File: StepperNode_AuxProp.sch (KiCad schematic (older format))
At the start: 4 parts

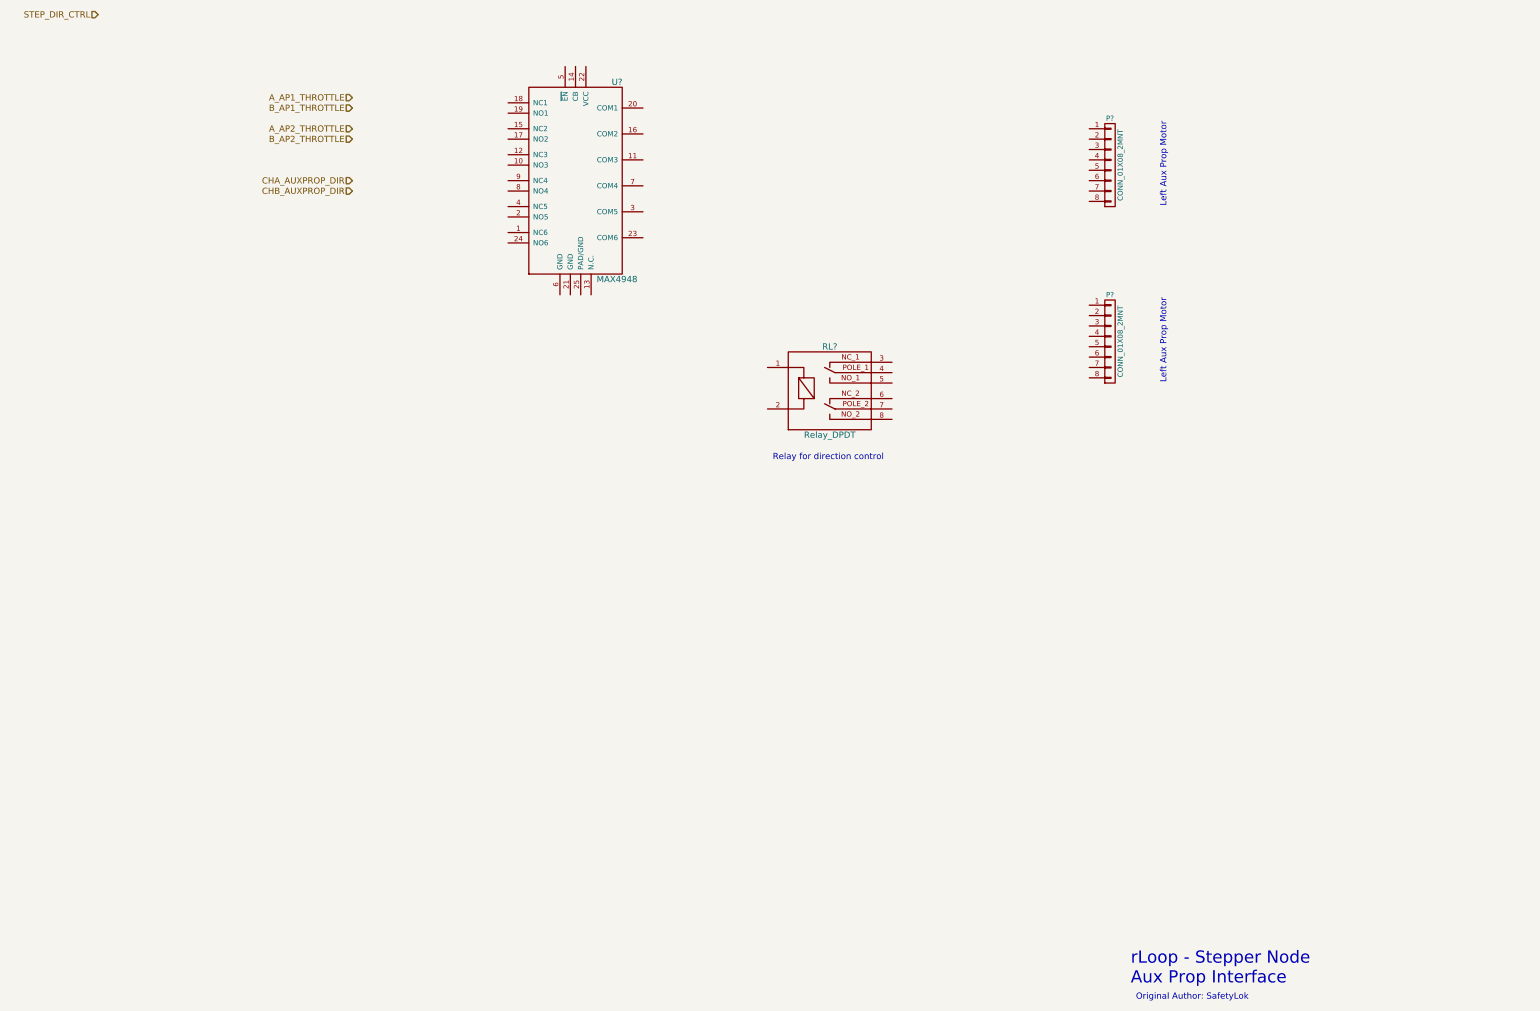
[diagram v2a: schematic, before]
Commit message: Update Stepper Temp Sensor Interface
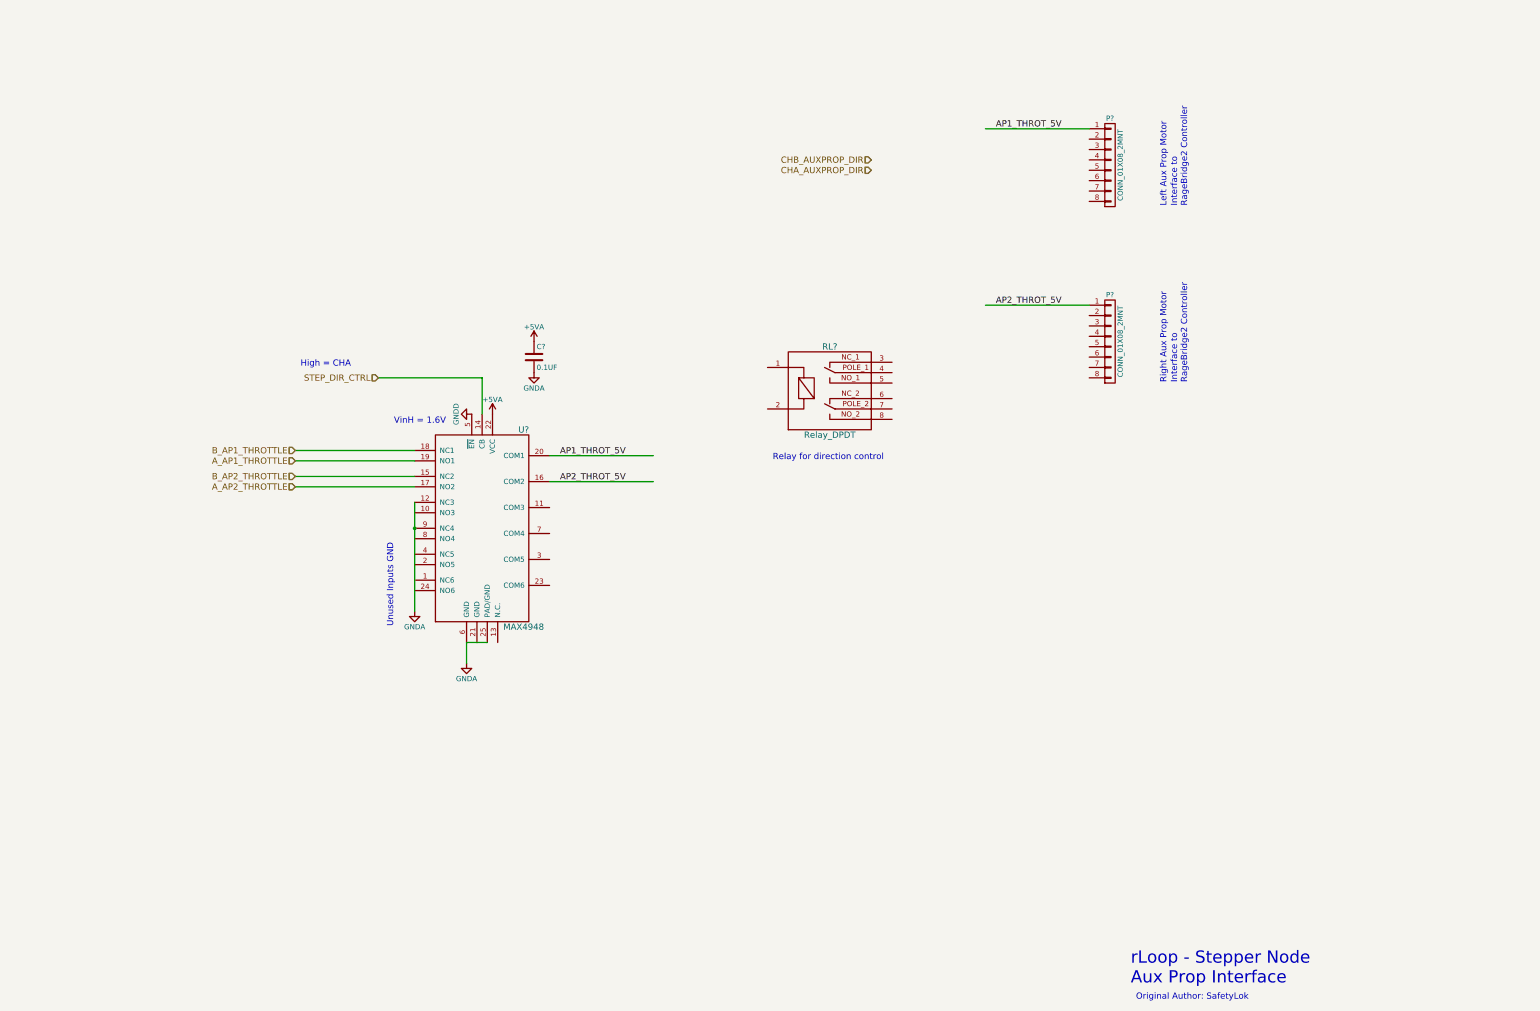
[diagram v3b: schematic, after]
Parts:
- added C?: 0.1UF, symbol C
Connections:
- net labels added: +5VA, AP1_THROT_5V, AP2_THROT_5V, GNDA, GNDD
- wire segments 0 -> 13
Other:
- note added: "High = CHA"
- note added: "Interface to \nRageBridge2 Controller"
- note added: "Right Aux Prop Motor"
- note added: "Unused Inputs GND"
- note added: "VinH = 1.6V"
- moved on the sheet: U?
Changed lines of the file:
@@
 $Descr A3 16535 11693
 encoding utf-8
-Sheet 16 17
+Sheet 15 17
 Title "Aux Propulsion Interface"
 Date ""
@@
 L MAX4948 U?
 U 1 1 575AE7BC
-P 6100 3500
-F 0 "U?" H 6950 5350 60  0000 C CNN
-F 1 "MAX4948" H 6950 3450 60  0000 C CNN
-F 2 "" H 6100 4250 60  0000 C CNN
-F 3 "" H 6100 4250 60  0000 C CNN
-	1    6100 3500
-	1    0    0    -1
-$EndComp
-Text HLabel 1950 1000 0    60   Input ~ 0
+P 5200 6850
+F 0 "U?" H 6050 8700 60  0000 C CNN
+F 1 "MAX4948" H 6050 6800 60  0000 C CNN
+F 2 "" H 5200 7600 60  0000 C CNN
+F 3 "" H 5200 7600 60  0000 C CNN
+	1    5200 6850
+	1    0    0    -1
+$EndComp
+Text HLabel 4650 4500 0    60   Input ~ 0
 STEP_DIR_CTRL
-Text HLabel 4400 1800 0    60   Input ~ 0
+Text HLabel 3850 5300 0    60   Input ~ 0
 A_AP1_THROTTLE
-Text HLabel 4400 1900 0    60   Input ~ 0
+Text HLabel 3850 5200 0    60   Input ~ 0
 B_AP1_THROTTLE
-Text HLabel 4400 2100 0    60   Input ~ 0
+Text HLabel 3850 5550 0    60   Input ~ 0
 A_AP2_THROTTLE
-Text HLabel 4400 2200 0    60   Input ~ 0
+Text HLabel 3850 5450 0    60   Input ~ 0
 B_AP2_THROTTLE
 $Comp
@@
 	1    0    0    -1
 $EndComp
-Text Notes 12250 4550 1    60   ~ 0
-Left Aux Prop Motor
 $Comp
 L Relay_DPDT RL?
@@
 Text Notes 8450 5300 0    60   ~ 0
 Relay for direction control
-Text HLabel 4400 2600 0    60   Input ~ 0
+Text HLabel 9400 2500 0    60   Input ~ 0
 CHA_AUXPROP_DIR
-Text HLabel 4400 2700 0    60   Input ~ 0
+Text HLabel 9400 2400 0    60   Input ~ 0
 CHB_AUXPROP_DIR
+$Comp
+L +5VA #PWR?
+U 1 1 5756511D
+P 5750 4850
+F 0 "#PWR?" H 5750 4700 50  0001 C CNN
+F 1 "+5VA" H 5750 4990 50  0000 C CNN
+F 2 "" H 5750 4850 50  0000 C CNN
+F 3 "" H 5750 4850 50  0000 C CNN
+	1    5750 4850
+	1    0    0    -1
+$EndComp
+$Comp
+L C C?
+U 1 1 57565139
+P 6150 4300
+F 0 "C?" H 6175 4400 50  0000 L CNN
+F 1 "0.1UF" H 6175 4200 50  0000 L CNN
+F 2 "" H 6188 4150 50  0000 C CNN
+F 3 "" H 6150 4300 50  0000 C CNN
+	1    6150 4300
+	1    0    0    -1
+$EndComp
+$Comp
+L +5VA #PWR?
+U 1 1 575651A0
+P 6150 4150
+F 0 "#PWR?" H 6150 4000 50  0001 C CNN
+F 1 "+5VA" H 6150 4290 50  0000 C CNN
+F 2 "" H 6150 4150 50  0000 C CNN
+F 3 "" H 6150 4150 50  0000 C CNN
+	1    6150 4150
+	1    0    0    -1
+$EndComp
+$Comp
+L GNDA #PWR?
+U 1 1 575651AF
+P 5000 6750
+F 0 "#PWR?" H 5000 6500 50  0001 C CNN
+F 1 "GNDA" H 5000 6600 50  0000 C CNN
+F 2 "" H 5000 6750 50  0000 C CNN
+F 3 "" H 5000 6750 50  0000 C CNN
+	1    5000 6750
+	1    0    0    -1
+$EndComp
+Text Notes 4800 4950 0    60   ~ 0
+VinH = 1.6V
+$Comp
+L GNDD #PWR?
+U 1 1 57565359
+P 5550 4850
+F 0 "#PWR?" H 5550 4600 50  0001 C CNN
+F 1 "GNDD" H 5550 4700 50  0000 C CNN
+F 2 "" H 5550 4850 50  0000 C CNN
+F 3 "" H 5550 4850 50  0000 C CNN
+	1    5550 4850
+	0    1    1    0
+$EndComp
+Wire Wire Line
+	5650 4850 5650 4500
+Wire Wire Line
+	5650 4500 4650 4500
+Text Notes 3900 4400 0    60   ~ 0
+High = CHA
+Wire Wire Line
+	5000 5200 3850 5200
+Wire Wire Line
+	5000 5300 3850 5300
+Wire Wire Line
+	5000 5450 3850 5450
+Wire Wire Line
+	5000 5550 3850 5550
+Wire Wire Line
+	5700 7050 5500 7050
+Wire Wire Line
+	5500 7050 5500 7250
+Wire Wire Line
+	5000 5700 5000 6750
+Text Notes 4800 6900 1    60   ~ 0
+Unused Inputs GND
+$Comp
+L GNDA #PWR?
+U 1 1 5756652B
+P 6150 4450
+F 0 "#PWR?" H 6150 4200 50  0001 C CNN
+F 1 "GNDA" H 6150 4300 50  0000 C CNN
+F 2 "" H 6150 4450 50  0000 C CNN
+F 3 "" H 6150 4450 50  0000 C CNN
+	1    6150 4450
+	1    0    0    -1
+$EndComp
+$Comp
+L GNDA #PWR?
+U 1 1 5756673C
+P 5500 7250
+F 0 "#PWR?" H 5500 7000 50  0001 C CNN
+F 1 "GNDA" H 5500 7100 50  0000 C CNN
+F 2 "" H 5500 7250 50  0000 C CNN
+F 3 "" H 5500 7250 50  0000 C CNN
+	1    5500 7250
+	1    0    0    -1
+$EndComp
+Text Notes 12450 2850 1    60   ~ 0
+Interface to \nRageBridge2 Controller
+Text Notes 12250 4550 1    60   ~ 0
+Right Aux Prop Motor
+Text Notes 12450 4550 1    60   ~ 0
+Interface to \nRageBridge2 Controller
+Connection ~ 5000 5950
+Wire Wire Line
+	6300 5250 7300 5250
+Text Label 6400 5250 0    60   ~ 0
+AP1_THROT_5V
+Wire Wire Line
+	6300 5500 7300 5500
+Text Label 6400 5500 0    60   ~ 0
+AP2_THROT_5V
+Wire Wire Line
+	10500 2100 11500 2100
+Text Label 10600 2100 0    60   ~ 0
+AP1_THROT_5V
+Wire Wire Line
+	10500 3800 11500 3800
+Text Label 10600 3800 0    60   ~ 0
+AP2_THROT_5V
 $EndSCHEMATC

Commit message: Updated node core connector pages and added interlocks.
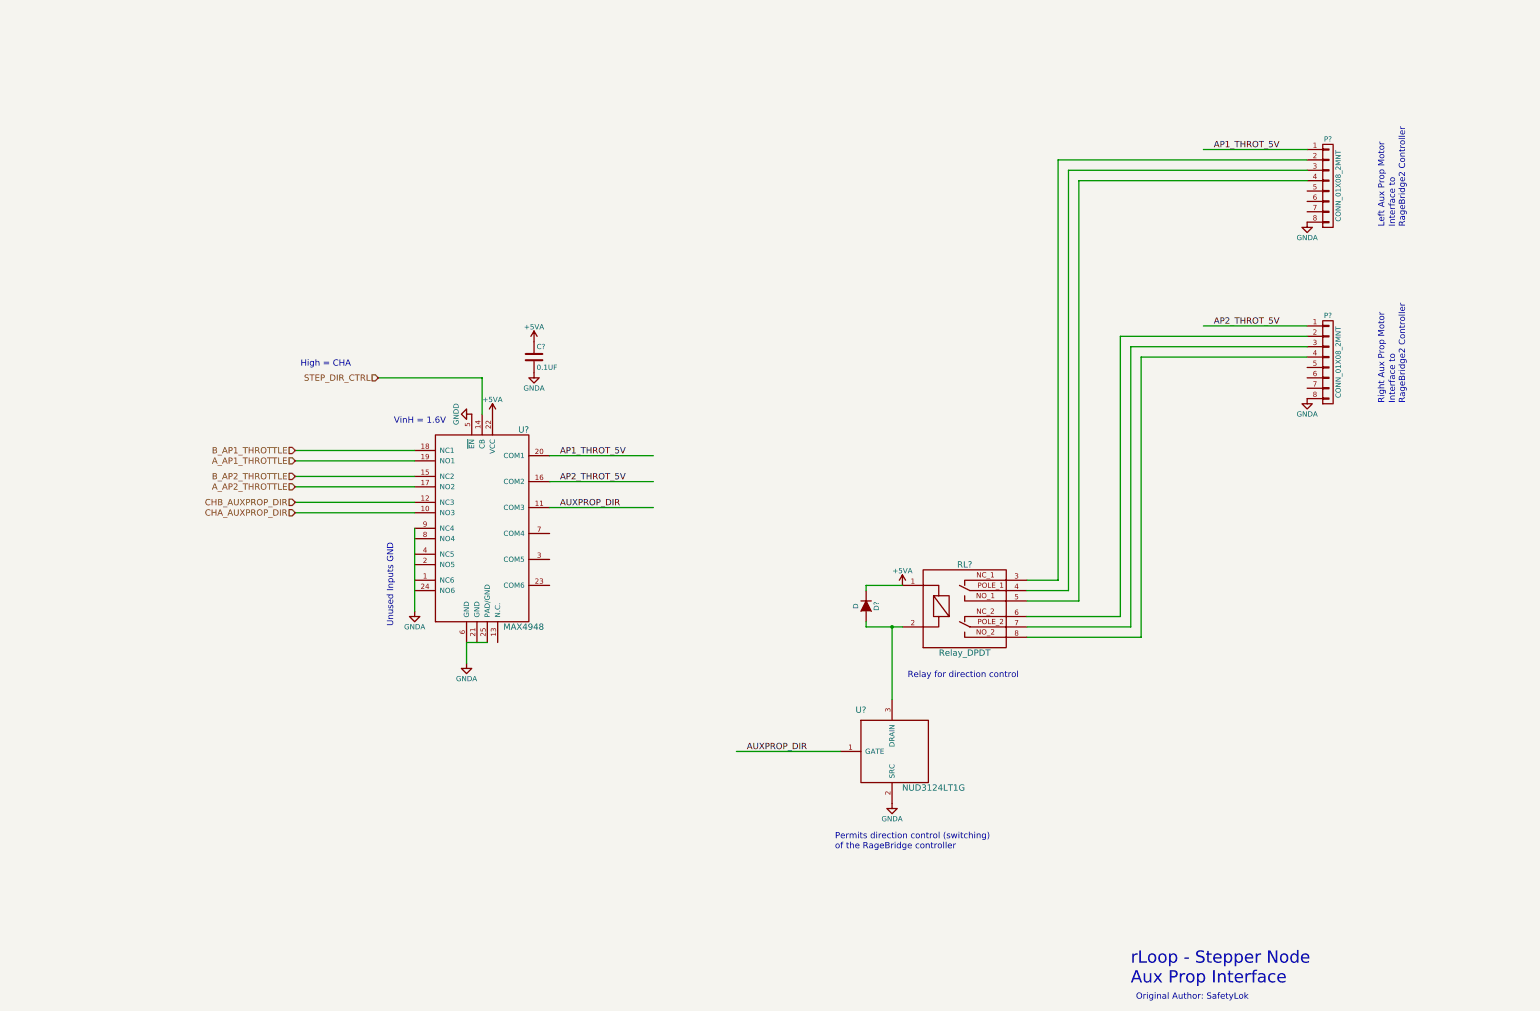
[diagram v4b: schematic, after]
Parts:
- added D?: D, symbol D
- added U?: NUD3124LT1G, symbol NUD3124LT1G
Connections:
- net labels added: AUXPROP_DIR
- wire segments 13 -> 40
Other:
- note added: "Permits direction control (switching)\nof the RageBridge controller"
- moved on the sheet: P?, RL?
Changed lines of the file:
@@
 L CONN_01X08_2MNT P?
 U 1 1 575AE559
-P 11700 2450
-F 0 "P?" H 11700 2900 50  0000 C CNN
-F 1 "CONN_01X08_2MNT" V 11800 2450 50  0000 C CNN
-F 2 "" H 11700 2450 50  0000 C CNN
-F 3 "" H 11700 2450 50  0000 C CNN
-	1    11700 2450
-	1    0    0    -1
-$EndComp
-Text Notes 12250 2850 1    60   ~ 0
+P 13800 2650
+F 0 "P?" H 13800 3100 50  0000 C CNN
+F 1 "CONN_01X08_2MNT" V 13900 2650 50  0000 C CNN
+F 2 "" H 13800 2650 50  0000 C CNN
+F 3 "" H 13800 2650 50  0000 C CNN
+	1    13800 2650
+	1    0    0    -1
+$EndComp
+Text Notes 14350 3050 1    60   ~ 0
 Left Aux Prop Motor
 $Comp
@@
 L CONN_01X08_2MNT P?
 U 1 1 575AEC09
-P 11700 4150
-F 0 "P?" H 11700 4600 50  0000 C CNN
-F 1 "CONN_01X08_2MNT" V 11800 4150 50  0000 C CNN
-F 2 "" H 11700 4150 50  0000 C CNN
-F 3 "" H 11700 4150 50  0000 C CNN
-	1    11700 4150
+P 13800 4350
+F 0 "P?" H 13800 4800 50  0000 C CNN
+F 1 "CONN_01X08_2MNT" V 13900 4350 50  0000 C CNN
+F 2 "" H 13800 4350 50  0000 C CNN
+F 3 "" H 13800 4350 50  0000 C CNN
+	1    13800 4350
 	1    0    0    -1
 $EndComp
@@
 L Relay_DPDT RL?
 U 1 1 575AEE52
-P 8600 5000
-F 0 "RL?" H 9000 5800 60  0000 C CNN
-F 1 "Relay_DPDT" H 9000 4950 60  0000 C CNN
-F 2 "" H 8600 5000 60  0000 C CNN
-F 3 "" H 8600 5000 60  0000 C CNN
-	1    8600 5000
-	1    0    0    -1
-$EndComp
-Text Notes 8450 5300 0    60   ~ 0
+P 9900 7100
+F 0 "RL?" H 10300 7900 60  0000 C CNN
+F 1 "Relay_DPDT" H 10300 7050 60  0000 C CNN
+F 2 "" H 9900 7100 60  0000 C CNN
+F 3 "" H 9900 7100 60  0000 C CNN
+	1    9900 7100
+	1    0    0    -1
+$EndComp
+Text Notes 9750 7400 0    60   ~ 0
 Relay for direction control
-Text HLabel 9400 2500 0    60   Input ~ 0
+Text HLabel 3850 5800 0    60   Input ~ 0
 CHA_AUXPROP_DIR
-Text HLabel 9400 2400 0    60   Input ~ 0
+Text HLabel 3850 5700 0    60   Input ~ 0
 CHB_AUXPROP_DIR
 $Comp
@@
 Wire Wire Line
 	5500 7050 5500 7250
-Wire Wire Line
-	5000 5700 5000 6750
 Text Notes 4800 6900 1    60   ~ 0
 Unused Inputs GND
@@
 	1    0    0    -1
 $EndComp
-Text Notes 12450 2850 1    60   ~ 0
+Text Notes 14550 3050 1    60   ~ 0
 Interface to \nRageBridge2 Controller
-Text Notes 12250 4550 1    60   ~ 0
+Text Notes 14350 4750 1    60   ~ 0
 Right Aux Prop Motor
-Text Notes 12450 4550 1    60   ~ 0
+Text Notes 14550 4750 1    60   ~ 0
 Interface to \nRageBridge2 Controller
-Connection ~ 5000 5950
 Wire Wire Line
 	6300 5250 7300 5250
@@
 AP2_THROT_5V
 Wire Wire Line
-	10500 2100 11500 2100
-Text Label 10600 2100 0    60   ~ 0
+	12600 2300 13600 2300
+Text Label 12700 2300 0    60   ~ 0
 AP1_THROT_5V
 Wire Wire Line
-	10500 3800 11500 3800
-Text Label 10600 3800 0    60   ~ 0
+	12600 4000 13600 4000
+Text Label 12700 4000 0    60   ~ 0
 AP2_THROT_5V
+Wire Wire Line
+	5000 5950 5000 6750
+Wire Wire Line
+	5000 5700 3850 5700
+Wire Wire Line
+	5000 5800 3850 5800
+Wire Wire Line
+	6300 5750 7300 5750
+Text Label 6400 5750 0    60   ~ 0
+AUXPROP_DIR
+$Comp
+L +5VA #PWR?
+U 1 1 575C0D8C
+P 9700 6500
+F 0 "#PWR?" H 9700 6350 50  0001 C CNN
+F 1 "+5VA" H 9700 6640 50  0000 C CNN
+F 2 "" H 9700 6500 50  0000 C CNN
+F 3 "" H 9700 6500 50  0000 C CNN
+	1    9700 6500
+	1    0    0    -1
+$EndComp
+Wire Wire Line
+	8100 8100 9100 8100
+Text Label 8200 8100 0    60   ~ 0
+AUXPROP_DIR
+$Comp
+L NUD3124LT1G U?
+U 1 1 575D421F
+P 9300 7800
+F 0 "U?" H 9300 7900 60  0000 C CNN
+F 1 "NUD3124LT1G" H 10000 7150 60  0000 C CNN
+F 2 "" H 9300 7800 60  0000 C CNN
+F 3 "" H 9300 7800 60  0000 C CNN
+	1    9300 7800
+	1    0    0    -1
+$EndComp
+$Comp
+L D D?
+U 1 1 575D425E
+P 9350 6700
+F 0 "D?" H 9350 6800 50  0000 C CNN
+F 1 "D" H 9350 6600 50  0000 C CNN
+F 2 "" H 9350 6700 50  0000 C CNN
+F 3 "" H 9350 6700 50  0000 C CNN
+	1    9350 6700
+	0    1    1    0
+$EndComp
+Wire Wire Line
+	9700 6500 9350 6500
+Wire Wire Line
+	9350 6500 9350 6550
+Wire Wire Line
+	9700 6900 9350 6900
+Wire Wire Line
+	9350 6900 9350 6850
+Wire Wire Line
+	9600 7600 9600 6900
+Connection ~ 9600 6900
+$Comp
+L GNDA #PWR?
+U 1 1 575D465A
+P 9600 8600
+F 0 "#PWR?" H 9600 8350 50  0001 C CNN
+F 1 "GNDA" H 9600 8450 50  0000 C CNN
+F 2 "" H 9600 8600 50  0000 C CNN
+F 3 "" H 9600 8600 50  0000 C CNN
+	1    9600 8600
+	1    0    0    -1
+$EndComp
+Text Notes 9050 9050 0    60   ~ 0
+Permits direction control (switching)\nof the RageBridge controller
+$Comp
+L GNDA #PWR?
+U 1 1 575D497D
+P 13600 3000
+F 0 "#PWR?" H 13600 2750 50  0001 C CNN
+F 1 "GNDA" H 13600 2850 50  0000 C CNN
+F 2 "" H 13600 3000 50  0000 C CNN
+F 3 "" H 13600 3000 50  0000 C CNN
+	1    13600 3000
+	1    0    0    -1
+$EndComp
+$Comp
+L GNDA #PWR?
+U 1 1 575D498C
+P 13600 4700
+F 0 "#PWR?" H 13600 4450 50  0001 C CNN
+F 1 "GNDA" H 13600 4550 50  0000 C CNN
+F 2 "" H 13600 4700 50  0000 C CNN
+F 3 "" H 13600 4700 50  0000 C CNN
+	1    13600 4700
+	1    0    0    -1
+$EndComp
+Wire Wire Line
+	13600 2400 11200 2400
+Wire Wire Line
+	11200 2400 11200 6450
+Wire Wire Line
+	11200 6450 10900 6450
+Wire Wire Line
+	10900 6550 11300 6550
+Wire Wire Line
+	11300 6550 11300 2500
+Wire Wire Line
+	11300 2500 13600 2500
+Wire Wire Line
+	10900 6650 11400 6650
+Wire Wire Line
+	11400 6650 11400 2600
+Wire Wire Line
+	11400 2600 13600 2600
+Wire Wire Line
+	10900 6800 11800 6800
+Wire Wire Line
+	11800 6800 11800 4100
+Wire Wire Line
+	11800 4100 13600 4100
+Wire Wire Line
+	10900 6900 11900 6900
+Wire Wire Line
+	11900 6900 11900 4200
+Wire Wire Line
+	11900 4200 13600 4200
+Wire Wire Line
+	10900 7000 12000 7000
+Wire Wire Line
+	12000 7000 12000 4300
+Wire Wire Line
+	12000 4300 13600 4300
 $EndSCHEMATC

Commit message: Update Max4948.
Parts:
- removed C?: 0.1UF, symbol C
- removed U?: MAX4948, symbol MAX4948
- added C?: C_100nF_50V, RLOOP_FOOTPRINTS:rLoop_C_0603, symbol C_100nF_50V
- added U?: MAX4948ETG+, RLOOP_FOOTPRINTS:rLoop_QFN24_4x4mm, symbol MAX4948ETG+
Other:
- note added: "TODO: CHECK ELECTRICAL ISOLATION OF RAGEBRIDGE CONTROLLER"
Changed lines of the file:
@@
 $Descr A3 16535 11693
 encoding utf-8
-Sheet 15 15
+Sheet 10 15
 Title "Aux Propulsion Interface"
 Date ""
@@
 Text Notes 14350 3050 1    60   ~ 0
 Left Aux Prop Motor
-$Comp
-L MAX4948 U?
-U 1 1 575AE7BC
-P 5200 6850
-F 0 "U?" H 6050 8700 60  0000 C CNN
-F 1 "MAX4948" H 6050 6800 60  0000 C CNN
-F 2 "" H 5200 7600 60  0000 C CNN
-F 3 "" H 5200 7600 60  0000 C CNN
-	1    5200 6850
-	1    0    0    -1
-$EndComp
 Text HLabel 4650 4500 0    60   Input ~ 0
 STEP_DIR_CTRL
@@
 $EndComp
 $Comp
-L C C?
-U 1 1 57565139
-P 6150 4300
-F 0 "C?" H 6175 4400 50  0000 L CNN
-F 1 "0.1UF" H 6175 4200 50  0000 L CNN
-F 2 "" H 6188 4150 50  0000 C CNN
-F 3 "" H 6150 4300 50  0000 C CNN
-	1    6150 4300
-	1    0    0    -1
-$EndComp
-$Comp
 L +5VA #PWR?
 U 1 1 575651A0
@@
 Wire Wire Line
 	12000 4300 13600 4300
+$Comp
+L MAX4948ETG+ U?
+U 1 1 575A2A8F
+P 5200 5050
+F 0 "U?" H 6050 5100 60  0000 C CNN
+F 1 "MAX4948ETG+" H 6250 3200 60  0000 C CNN
+F 2 "RLOOP_FOOTPRINTS:rLoop_QFN24_4x4mm" H 5200 4000 60  0001 C CNN
+F 3 "" H 5200 4000 60  0000 C CNN
+	1    5200 5050
+	1    0    0    -1
+$EndComp
+$Comp
+L C_100nF_50V C?
+U 1 1 575A2AEB
+P 6150 4300
+F 0 "C?" H 6175 4400 50  0000 L CNN
+F 1 "C_100nF_50V" H 6175 4200 50  0000 L CNN
+F 2 "RLOOP_FOOTPRINTS:rLoop_C_0603" H 6188 4150 50  0001 C CNN
+F 3 "" H 6150 4300 50  0000 C CNN
+	1    6150 4300
+	1    0    0    -1
+$EndComp
+Text Notes 8850 1700 0    118  ~ 0
+TODO: CHECK ELECTRICAL ISOLATION OF RAGEBRIDGE CONTROLLER
 $EndSCHEMATC
